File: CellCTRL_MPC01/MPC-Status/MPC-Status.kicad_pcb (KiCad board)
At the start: 4 copper layers, 70 x 70 mm, 35 parts, among them J1 Programming, J2 I2C, J3 Reset, U1 ATtiny202-SS

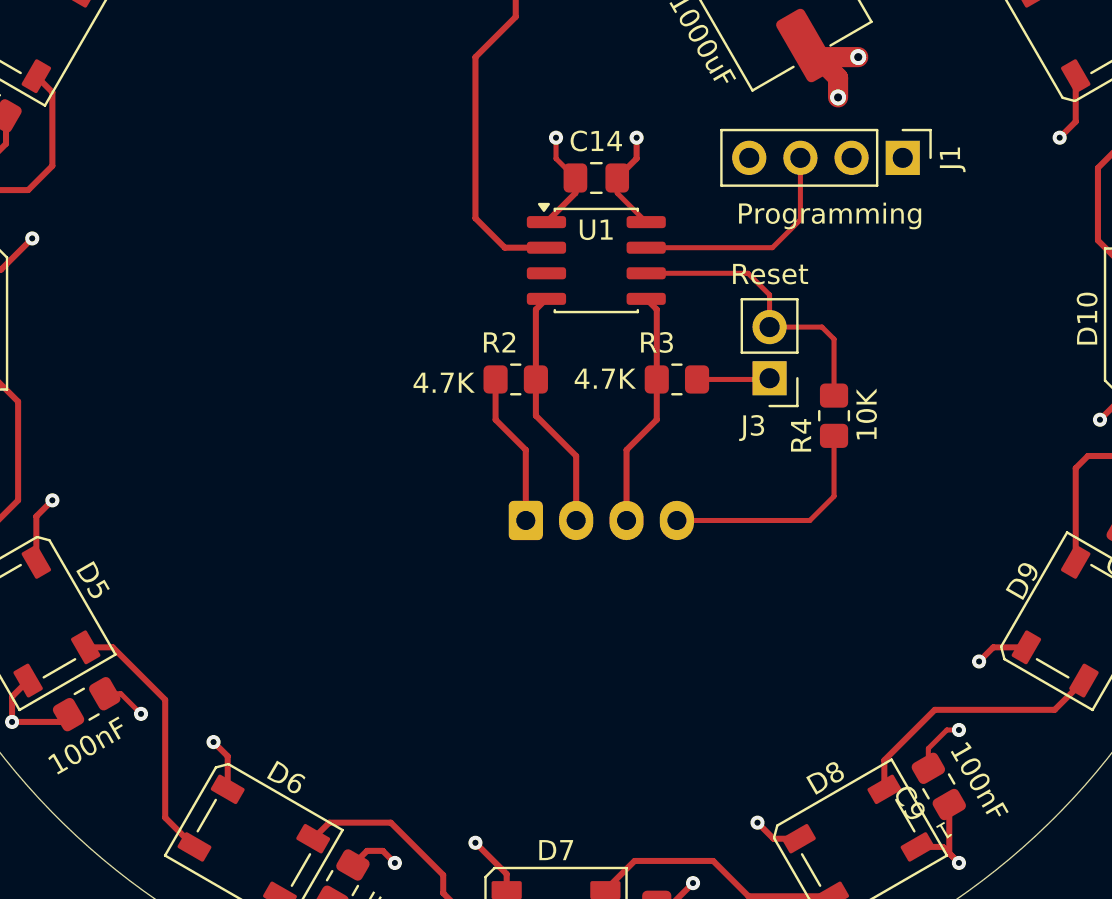
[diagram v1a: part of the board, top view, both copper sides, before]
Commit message: Mounting Hole adds
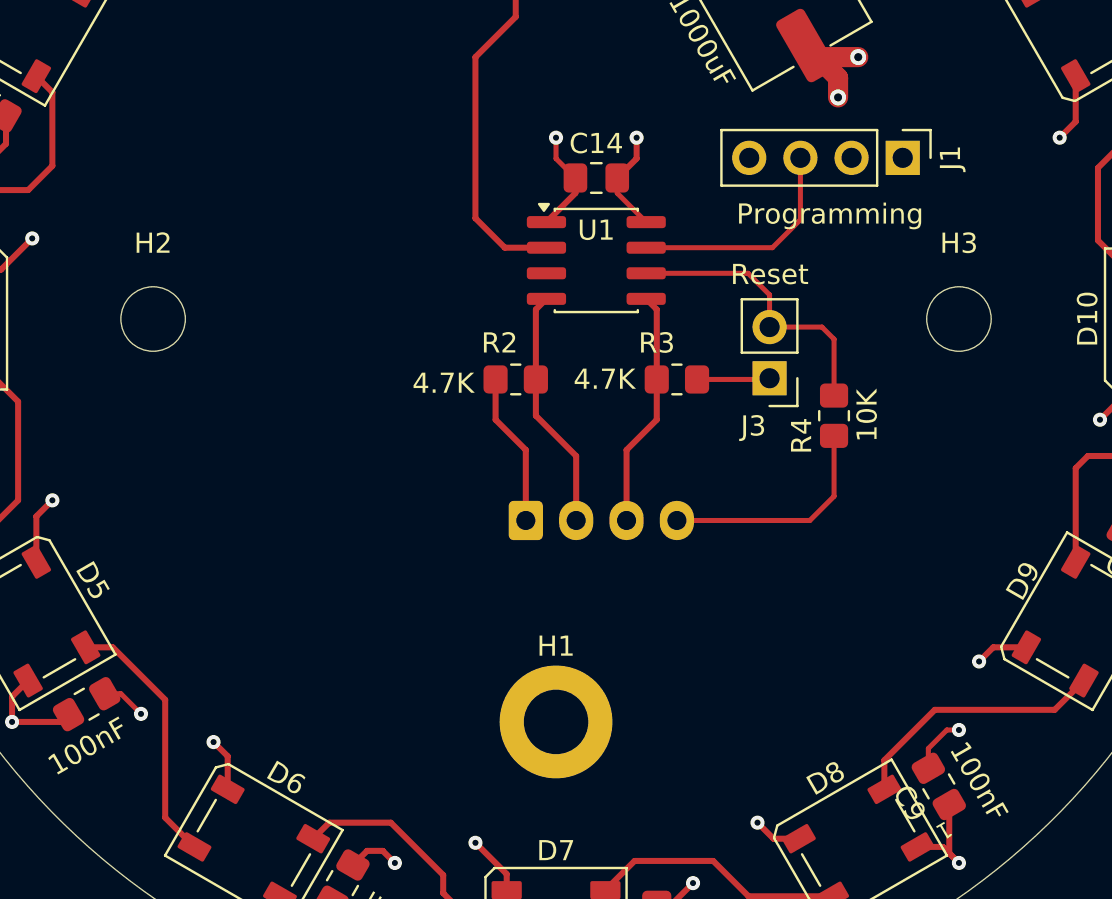
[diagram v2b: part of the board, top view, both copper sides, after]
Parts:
- added H1: MountingHole_Pad, MountingHole:MountingHole_3.2mm_M3_DIN965_Pad, F.Cu at (150.0, 125.0)
- added H2: MountingHole, MountingHole:MountingHole_3.2mm_M3_DIN965, F.Cu at (130.0, 105.0)
- added H3: MountingHole, MountingHole:MountingHole_3.2mm_M3_DIN965, F.Cu at (170.0, 105.0)

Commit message: Fertig V0.1_Status
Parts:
- H2, H3: value MountingHole -> MountingHole_Pad; footprint MountingHole:MountingHole_3.2mm_M3_DIN965 -> MountingHole:MountingHole_3.2mm_M3_DIN965_Pad
- J2: footprint Connector_JST:JST_EH_B4B-EH-A_1x04_P2.50mm_Vertical -> Connector_JST:JST_XH_B4B-XH-A_1x04_P2.50mm_Vertical
- moved R4 1.20 mm to (165.0, 109.8)
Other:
- board text added: "1A"
- board text added: "5V"
- board text added: "GND"
- board text added: "MPC-Status"
- board text added: "PROG"
- board text added: "RESET"
- board text added: "SCL"
- board text added: "SDA"
- board text added: "V 0.1 03/2026 Kappi084 github.com/Kappi084"
